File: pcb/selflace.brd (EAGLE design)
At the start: 100 x 80 mm, 17 parts, among them J3 AVR_SPI_PROG_3X2NS, U1 ATMEGA328P_TQFP

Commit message: sending sch off for review
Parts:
- added C6: 0.33µF, SparkFun-Capacitors:0805
- added C7: 0.1uF, SparkFun-Capacitors:0603
- added C8, C9: 22pF, SparkFun-Capacitors:0603
- added IC1: 7805T, adafruit:TO220H
- added J5: (no value), SparkFun-Connectors:1X02
- added J6: (no value), SparkFun-Connectors:JST-2-PTH
- added J7: (no value), SparkFun-Connectors:1X03
- added R6, R7: 10k, SparkFun-Resistors:0603
- added S1: MOMENTARY-SWITCH-SPST-PTH-6.0MM, SparkFun-Switches:TACTILE_SWITCH_PTH_6.0MM
- added VR1: 10k, SparkFun-Resistors:POT-PTH-ALPS
- added Y1: 16MHz, SparkFun-Clocks:HC49US
- R5: value 1k -> 10k
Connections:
- new net DIG5: U1.9, U2.P$2
- new net DIG6: U1.10, U2.P$3
- new net N$1: R6.2, S1.1, U1.2
- new net N$11: C9.1, U1.8, Y1.1
- new net N$12: C6.1, IC1.1, J6.1, J7.3
- new net N$2: J5.2, R7.2, U1.11
- net GND: now also C6.2, C7.2, C8.2, C9.2, IC1.2, J6.2, J7.2, R6.1, R7.1, VR1.P$3
- net N$6: now also U1.25, VR1.P$2; no longer U1.13, U2.P$3
- net N$7: now also C8.1, U1.7, Y1.2; no longer U1.14, U2.P$2
- net VCC: now also C7.1, IC1.3, J5.1, S1.3, U1.20, VR1.P$1
- net VCC_1: now also J7.1

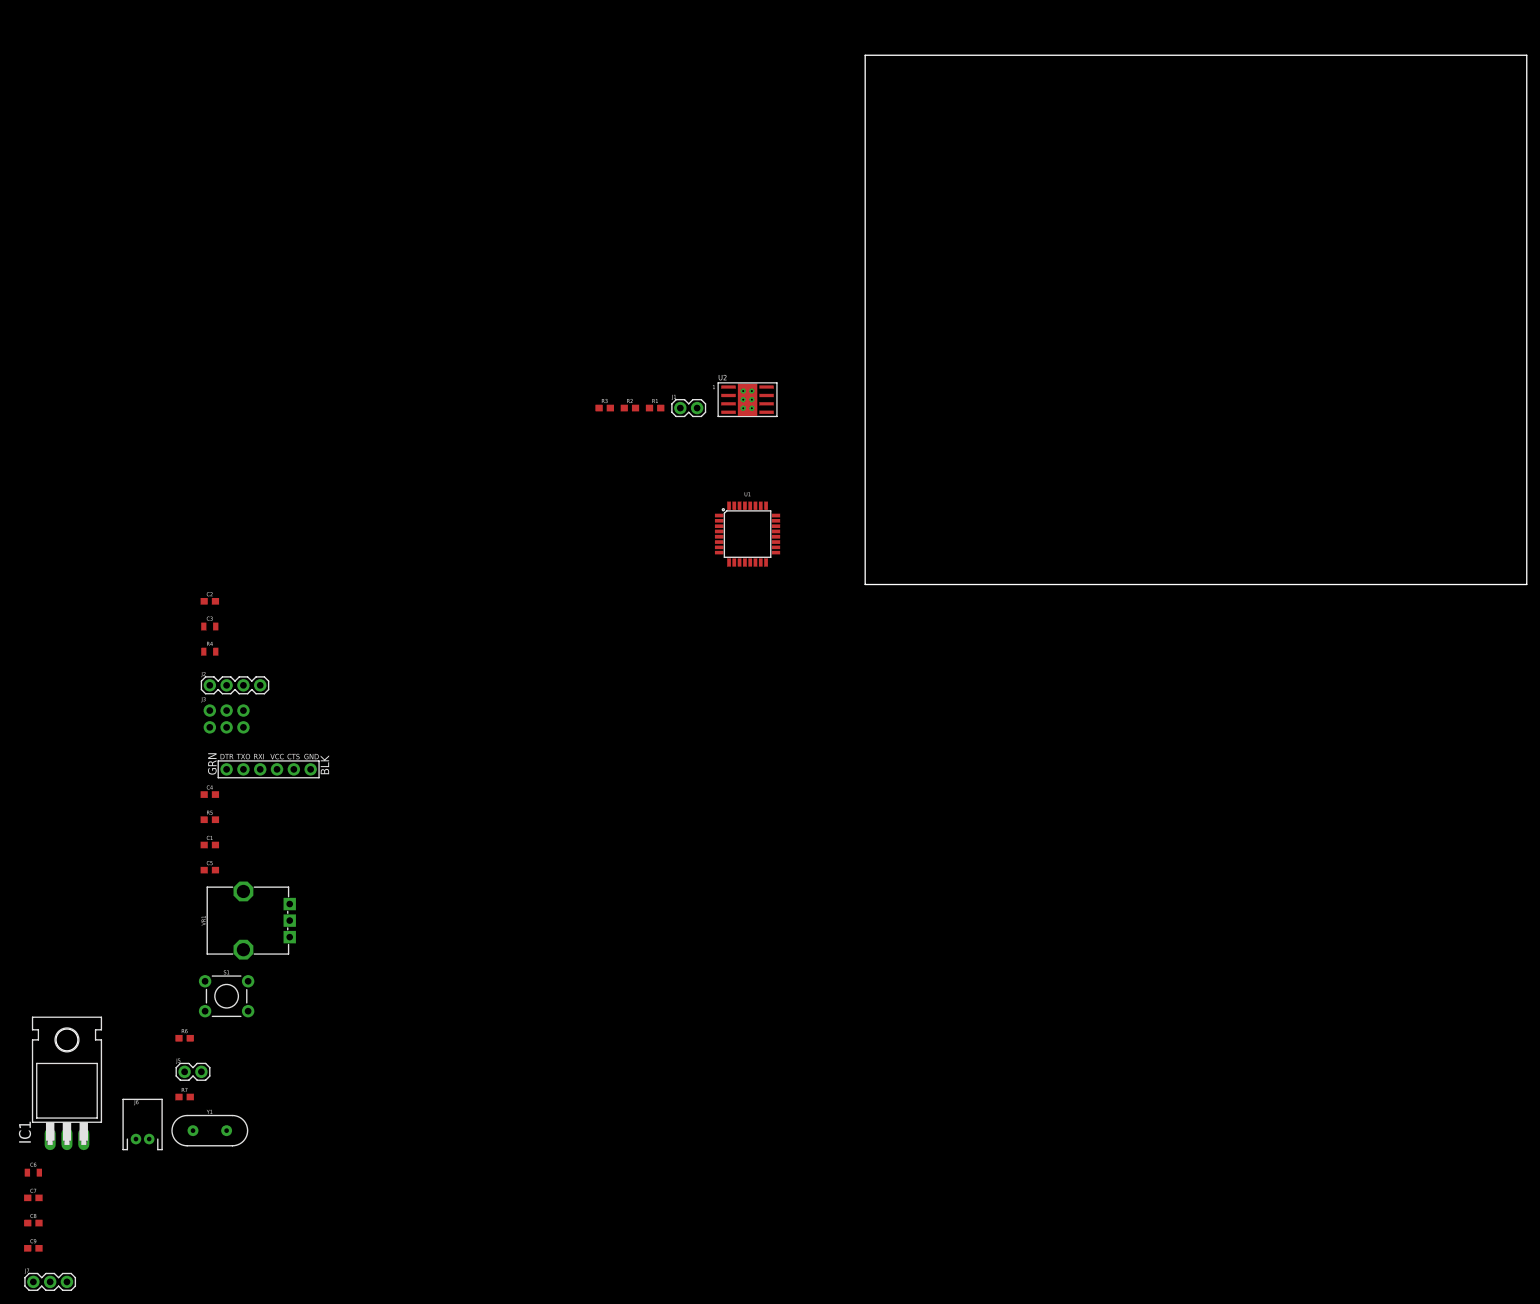
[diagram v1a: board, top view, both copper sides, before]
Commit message: maybe finish schematic, sending off for review
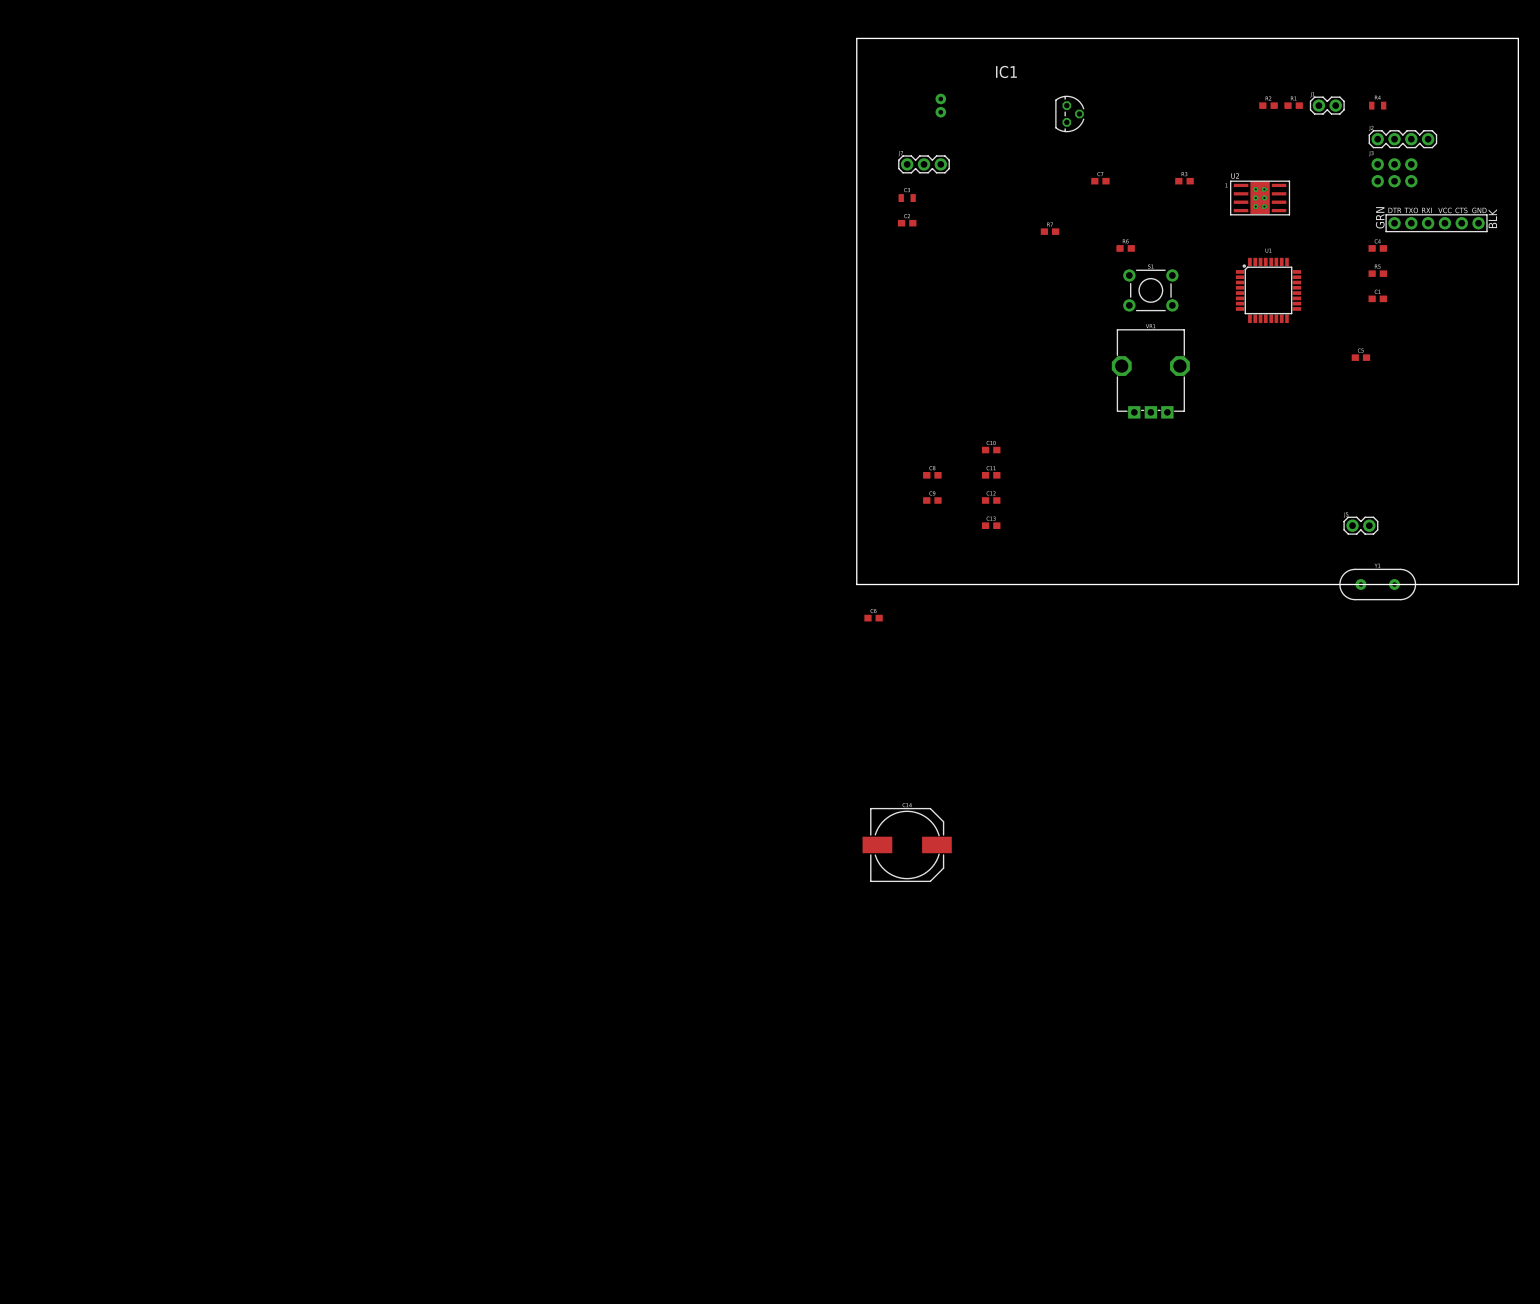
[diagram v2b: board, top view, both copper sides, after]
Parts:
- added C10, C12: 1.0uF, SparkFun-Capacitors:0603
- added C11, C13: 0.1uF, SparkFun-Capacitors:0603
- added C14: 100uF, SparkFun-Capacitors:NIC_10X10.5_CAP
- C6: value 0.33µF -> 1.0uF; device SparkFun-Capacitors:0805 -> SparkFun-Capacitors:0603
- IC1: value 7805T -> 78L05Z; device adafruit:TO220H -> linear:TO92
- moved C7 222.8 mm to (35.6, 61.0)
- moved J7 214.4 mm to (6.35, 63.5)
- moved IC1 209.3 mm to (30.5, 71.1), turned to 270 degrees
- moved J6 197.4 mm to (11.4, 72.4), flipped to the bottom, turned to 270 degrees
- moved C1 194.9 mm to (77.5, 43.2)
- moved C4 194.9 mm to (77.5, 50.8)
- moved J2 194.9 mm to (77.5, 67.3)
- moved J3 194.9 mm to (80.0, 62.2)
- moved J4 194.9 mm to (86.4, 54.6)
- moved J5 194.9 mm to (73.7, 8.89)
- moved R4 194.9 mm to (77.5, 72.4)
- moved R5 194.9 mm to (77.5, 47.0)
- moved Y1 194.9 mm to (77.5, 0.00)
- moved C5 190.5 mm to (74.9, 34.3)
- moved R6 185.7 mm to (39.4, 50.8)
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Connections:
- net GND: now also C10.2, C11.2, C12.2, C13.2, C14.-, C6.1, J6.1; no longer C6.2, J6.2
- net N$12: now also C14.+, C6.2, IC1.3, J6.2; no longer C6.1, IC1.1, J6.1
- net N$3: now also R3.1; no longer R3.2
- net VCC: now also C10.1, C11.1, C12.1, C13.1, IC1.1, R3.2; no longer IC1.3, R3.1
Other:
- board size 100 x 80 mm -> 100 x 82.5 mm

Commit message: nearly done! sending off for final review
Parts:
- added C15: 0.1uF, SparkFun-Capacitors:0603
- added D1: FWD, SparkFun-LED:LED-1206
- added D2: BKWD, SparkFun-LED:LED-1206
- added D3: POWER, SparkFun-LED:LED-1206
- added D4: STATE, SparkFun-LED:LED-1206
- added LOGO1: OSHW-LOGOM, SparkFun-Aesthetics:OSHW-LOGO-M
- added MGT1, MGT2, MGT3, MGT4: BEAGLEBONEBLACK_MOUNTING_HOLE, BeagleBone_Black_Wireless:BEAGLEBONEBLACK_MOUNTING_HOLE
- added R10, R11, R8, R9: 220, SparkFun-Resistors:0603
- moved C14 118.1 mm to (40.6, 73.7), turned to 180 degrees
- moved C6 79.8 mm to (20.3, 72.4)
- moved Y1 66.1 mm to (36.8, 52.1), turned to 90 degrees
- moved J4 60.8 mm to (33.0, 83.8), turned to 180 degrees
- moved R4 58.2 mm to (27.9, 41.9)
- moved C13 56.4 mm to (16.5, 65.3), turned to 90 degrees
- moved J3 53.0 mm to (29.2, 77.5)
- moved C5 52.8 mm to (30.7, 63.1), turned to 90 degrees
- moved C12 52.7 mm to (14.9, 65.3), turned to 90 degrees
- moved C1 52.3 mm to (29.1, 63.1), turned to 90 degrees
- moved J5 52.1 mm to (44.5, 52.1), turned to 90 degrees
- moved R5 51.2 mm to (30.5, 67.3), turned to 90 degrees
- moved C4 50.6 mm to (31.8, 72.4), turned to 180 degrees
- moved C8 49.8 mm to (40.6, 55.9), turned to 270 degrees
- moved C9 46.8 mm to (40.6, 48.3), turned to 90 degrees
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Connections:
- new net DIG2: R8.1, U1.32
- new net DIG3: R9.1, U1.1
- new net DIG8: R10.1, U1.12
- new net DIG9: R11.1, U1.13
- new net N$13: D1.A, R8.2
- new net N$14: D2.A, R9.2
- new net N$15: D3.A, R10.2
- new net N$16: D4.A, R11.2
- net GND: now also C15.2, D1.C, D2.C, D3.C, D4.C, MGT1.P$1, MGT2.P$1, MGT3.P$1, MGT4.P$1
- net VCC: now also C15.1
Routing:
- net GND: track 0.00 -> 309.1 mm
- net VCC: track 0.00 -> 179.3 mm, vias 0 -> 5
- net N$12: track 0.00 -> 63.8 mm, vias 0 -> 1
- net N$2: track 0.00 -> 58.2 mm
- net VCC_1: track 0.00 -> 52.7 mm, vias 0 -> 2
- net MOSI: track 0.00 -> 28.6 mm, vias 0 -> 1
- net N$11: track 0.00 -> 27.6 mm, vias 0 -> 1
- net DIG8: track 0.00 -> 27.1 mm, vias 0 -> 2
- net N$4: track 0.00 -> 26.6 mm
- net RESET: track 0.00 -> 26.4 mm
- net N$6: track 0.00 -> 26.3 mm, vias 0 -> 1
- net N$7: track 0.00 -> 25.9 mm, vias 0 -> 2
- net RX: track 0.00 -> 25.4 mm
- net TX: track 0.00 -> 24.1 mm, vias 0 -> 1
- net N$5: track 0.00 -> 24.0 mm, vias 0 -> 1
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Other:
- board size 100 x 82.5 mm -> 50.5 x 52.1 mm
- board text added: "(c) Skyler Cleland, Hazel Levine"
- board text added: "BKW"
- board text added: "BOOST"
- board text added: "FSR"
- board text added: "FWD"
- board text added: "LIMIT"
- board text added: "MOTOR"
- board text added: "PWR"
- board text added: "STAT"
- board text added: "Self-Lacing Shoe -- DE 2019"

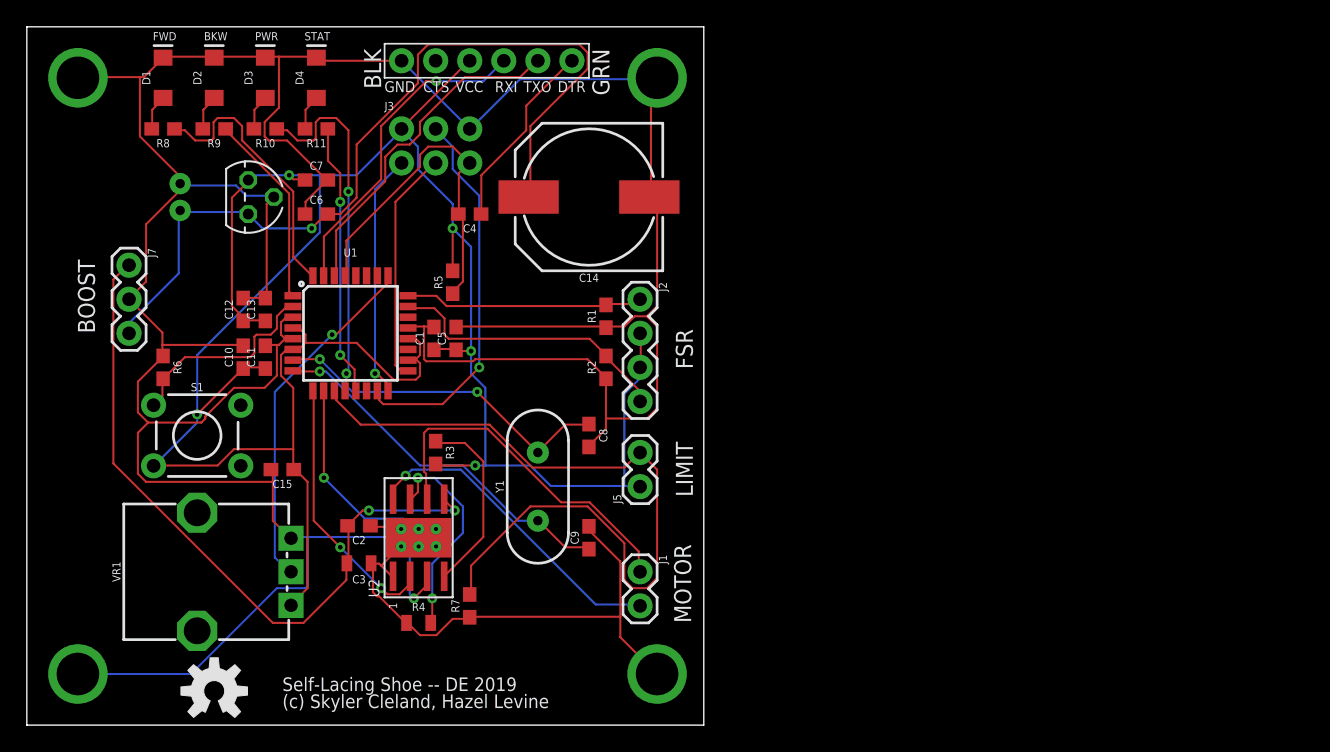
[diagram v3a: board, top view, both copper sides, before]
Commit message: add LEDs
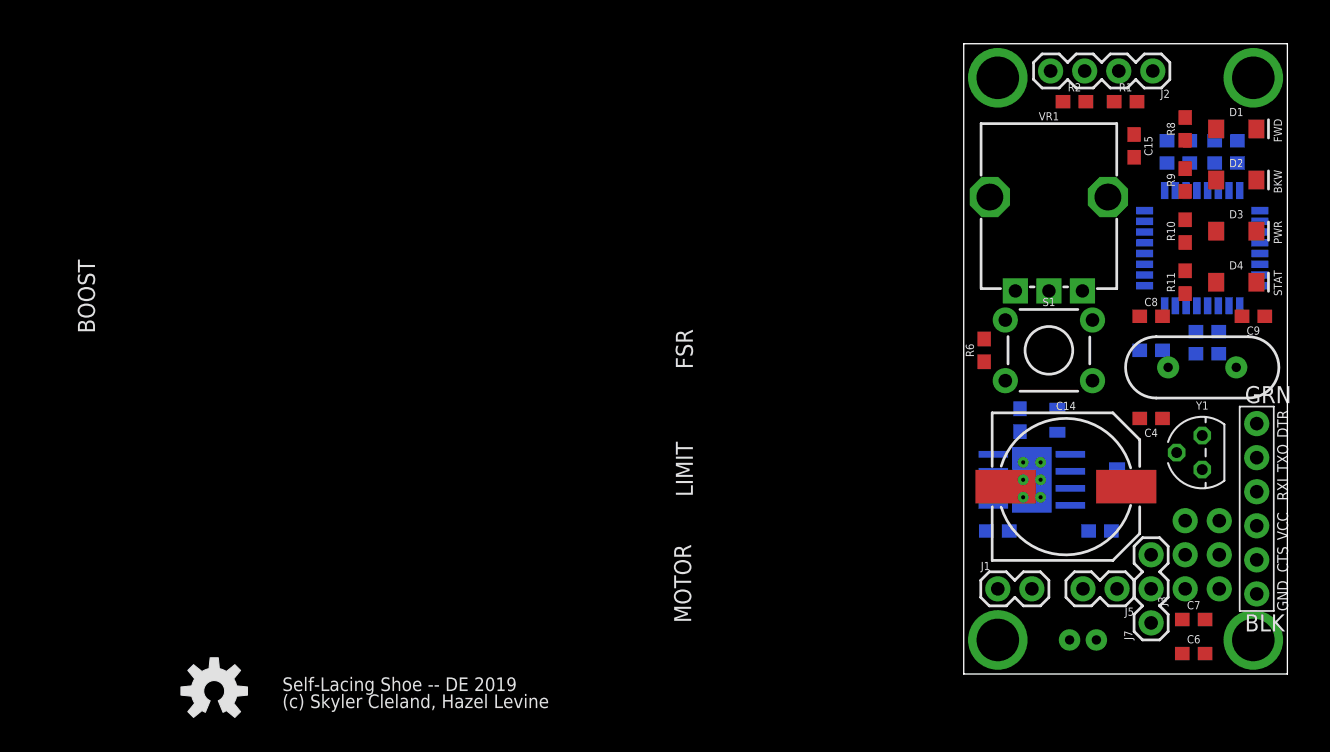
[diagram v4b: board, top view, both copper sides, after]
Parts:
- moved J7 80.7 mm to (82.5, 41.9), turned to 90 degrees
- moved D1 80.1 mm to (88.9, 78.7), turned to 0 degrees
- moved D2 76.6 mm to (88.9, 74.9), turned to 0 degrees
- moved R8 76.2 mm to (85.1, 78.7), turned to 90 degrees
- moved C10 75.0 mm to (88.1, 77.9), flipped to the bottom, turned to 0 degrees
- moved J6 75.0 mm to (77.5, 40.6), turned to 180 degrees
- moved IC1 73.6 mm to (86.4, 54.6), turned to 90 degrees
- moved D3 73.3 mm to (88.9, 71.1), turned to 0 degrees
- moved C6 73.2 mm to (85.7, 39.6)
- moved C7 73.2 mm to (85.7, 42.2)
- moved C11 73.1 mm to (88.1, 76.2), flipped to the bottom, turned to 0 degrees
- moved R9 72.5 mm to (85.1, 74.9), turned to 90 degrees
- moved C12 70.8 mm to (84.6, 77.9), flipped to the bottom, turned to 0 degrees
- moved D4 70.3 mm to (88.9, 67.3), turned to 0 degrees
- moved VR1 69.4 mm to (74.9, 73.7), turned to 270 degrees
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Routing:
- net GND: track 309.1 -> 0.00 mm
- net VCC: track 179.3 -> 0.00 mm, vias 5 -> 0
- net N$12: track 63.8 -> 0.00 mm, vias 1 -> 0
- net N$2: track 58.2 -> 0.00 mm
- net VCC_1: track 52.7 -> 0.00 mm, vias 2 -> 0
- net MOSI: track 28.6 -> 0.00 mm, vias 1 -> 0
- net N$11: track 27.6 -> 0.00 mm, vias 1 -> 0
- net DIG8: track 27.1 -> 0.00 mm, vias 2 -> 0
- net N$4: track 26.6 -> 0.00 mm
- net RESET: track 26.4 -> 0.00 mm
- net N$6: track 26.3 -> 0.00 mm, vias 1 -> 0
- net N$7: track 25.9 -> 0.00 mm, vias 2 -> 0
- net RX: track 25.4 -> 0.00 mm
- net TX: track 24.1 -> 0.00 mm, vias 1 -> 0
- net N$5: track 24.0 -> 0.00 mm, vias 1 -> 0
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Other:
- board size 50.5 x 52.1 mm -> 24.1 x 47 mm
